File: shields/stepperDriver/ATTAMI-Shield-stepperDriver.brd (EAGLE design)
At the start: 22.5 x 30.5 mm, 16 parts, among them CN1 1X4-BIG

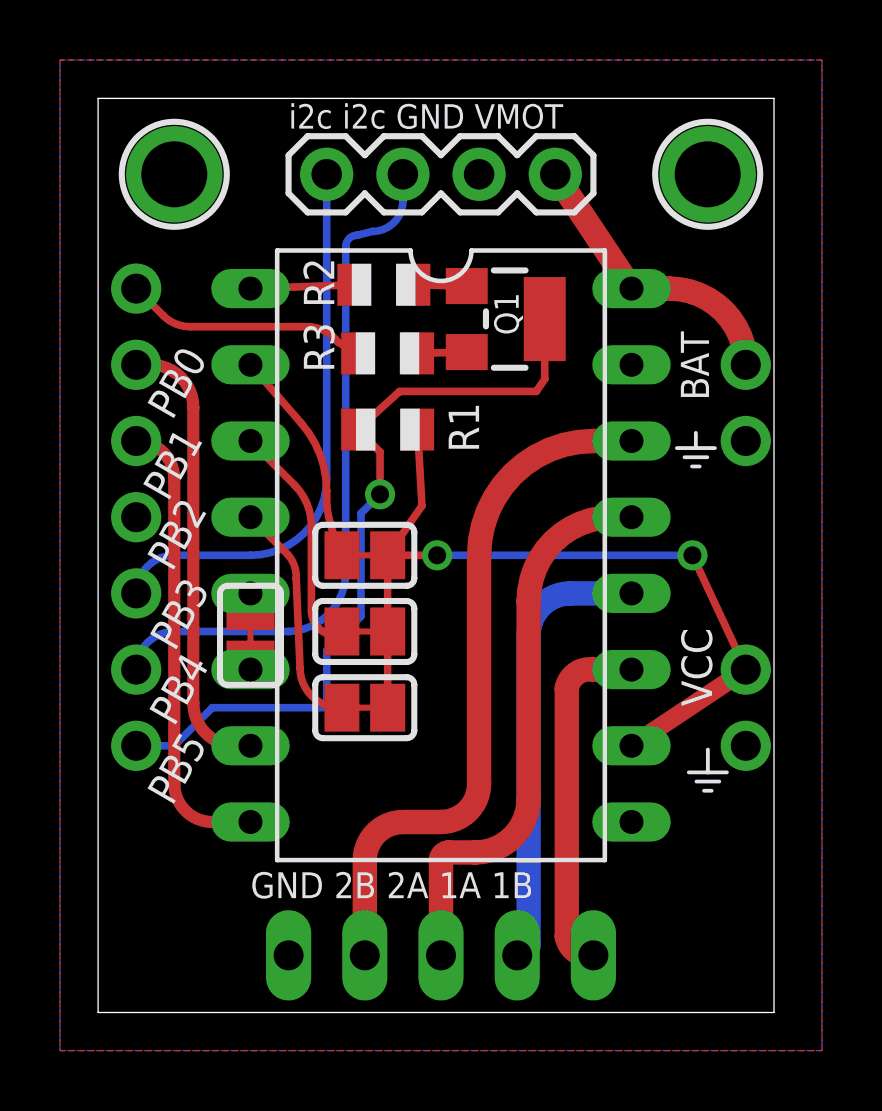
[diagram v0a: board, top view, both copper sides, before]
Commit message: simplfy
this is a driver design we need a barebone onn with High Speed
Optoisolator SOIC 16 , 60V 4A.
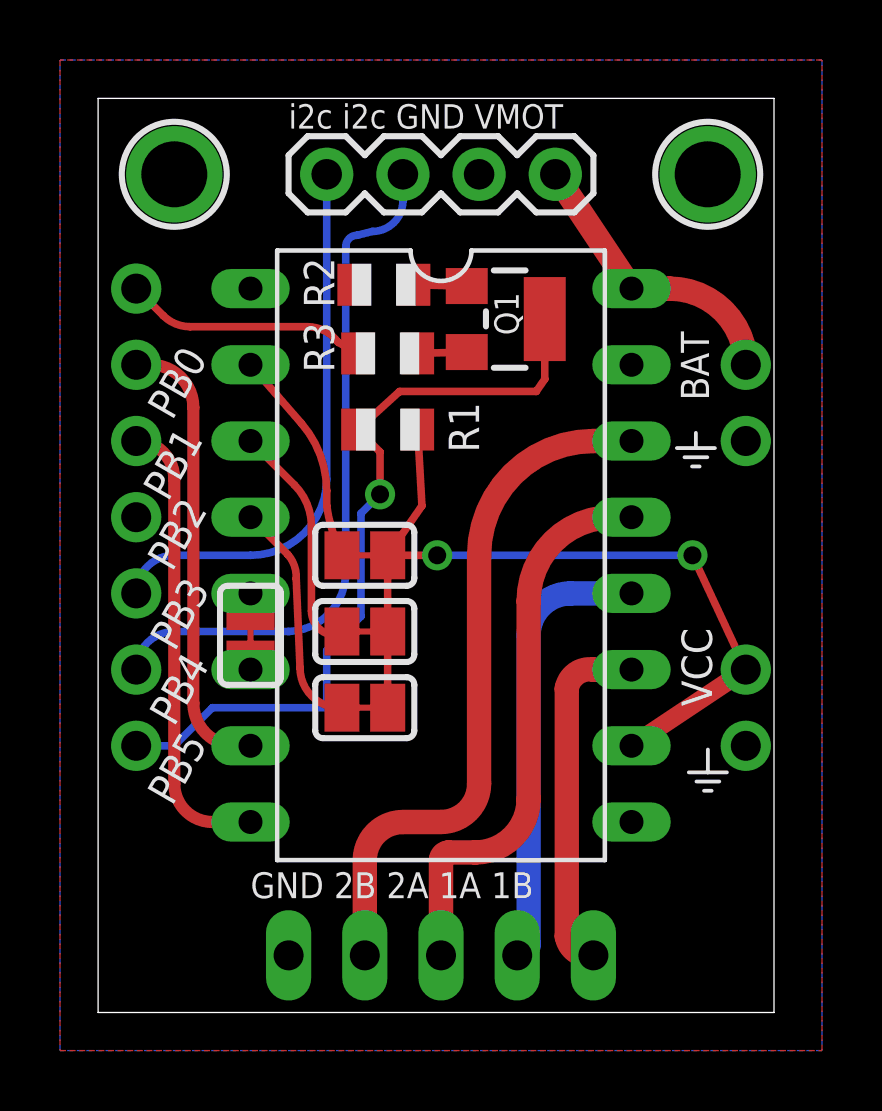
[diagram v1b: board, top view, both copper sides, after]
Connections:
- removed net ENABLE: BRK1.1, R2.1
- net PB2: now also BRK1.1
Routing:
- net ENABLE: track 3.45 -> 0.00 mm
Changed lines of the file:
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@@
 <signal name="PB2">
 <contactref element="J1" pad="4"/>
+<contactref element="BRK1" pad="1"/>
+<wire x1="1.27" y1="16.51" x2="5.08" y2="24.13" width="0" layer="19" extent="1-1"/>
 </signal>
 <signal name="PB3">
@@
 <wire x1="10.525" y1="24.257" x2="12.289" y2="24.214" width="0.254" layer="1"/>
 </signal>
-<signal name="ENABLE">
-<contactref element="R2" pad="1"/>
-<contactref element="BRK1" pad="1"/>
-<wire x1="5.08" y1="24.13" x2="8.525" y2="24.257" width="0.254" layer="1"/>
-</signal>
 <signal name="N$10">
